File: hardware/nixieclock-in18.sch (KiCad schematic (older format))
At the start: 19 parts

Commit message: pcb begins
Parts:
- removed U?: TL071, symbol Amplifier_Operational:TL071
- added BT1: CR2032, Battery_Holders:Keystone_103_1x20mm-CoinCell, symbol Device:Battery_Cell
- added C1, C2, C3: 0.1, Capacitors_SMD:C_0805_HandSoldering, symbol Device:C
- added C4: 1.0, Capacitors_SMD:C_0805_HandSoldering, symbol Device:C
- added D1: LED, LEDs:LED_D3.0mm_FlatTop, symbol Device:LED
- added D4, D5, D6, D7: 3v3, Diodes_THT:D_DO-41_SOD81_P7.62mm_Horizontal, symbol Device:D_Zener
- added J1: PROG, Pin_Headers:Pin_Header_Straight_1x07_Pitch2.54mm, symbol Connector_Generic:Conn_01x06
- added J2: POWER, Connectors_Terminal_Blocks:TerminalBlock_bornier-2_P5.08mm, symbol Connector:Screw_Terminal_01x02
- added Q10, Q11, Q12, Q13, Q14, Q15, Q16, Q17, Q18, Q19, Q20, Q21, Q4, Q5, Q6, Q7, Q8, Q9: MPSA42, TO_SOT_Packages_SMD:SOT-23_Handsoldering, symbol Transistor_BJT:MPSA42
- added R1: 200, Resistors_SMD:R_0805_HandSoldering, symbol Device:R
- added R10, R12, R14, R15, R17, R19, R20, R21, R23, R25, R26, R28, R30, R9: 8k2, Resistors_SMD:R_0805_HandSoldering, symbol Device:R
- added R11, R16, R22, R27: 200k, Resistors_SMD:R_0805_HandSoldering, symbol Device:R
- added R13, R18, R24, R29: 27k, Resistors_SMD:R_0805_HandSoldering, symbol Device:R
- added R5: 10k, Resistors_SMD:R_0805_HandSoldering, symbol Device:R
- added T1, T2, T3, T4: IN18, in18:IN18, symbol in18:IN18
- added U1: LM1117-3.3, TO_SOT_Packages_SMD:SOT-223, symbol Regulator_Linear:LM1117-3.3
- added U2: DS3231M, Housings_SOIC:SOIC-16W_7.5x10.3mm_Pitch1.27mm, symbol Timer_RTC:DS3231M
- added U3: LM393, Housings_SOIC:SOIC-8_3.9x4.9mm_Pitch1.27mm, symbol Comparator:LM393
- C5, C6, C8: renamed from C?; footprint (none) -> Capacitors_SMD:C_0805_HandSoldering
- C7: renamed from C?; value 2.2uF -> 1.0; footprint (none) -> Capacitors_THT:CP_Radial_D10.0mm_P5.00mm
- D2: renamed from D?; footprint (none) -> Diodes_THT:D_A-405_P10.16mm_Horizontal
- D3: renamed from D?; footprint (none) -> Diodes_THT:D_DO-41_SOD81_P7.62mm_Horizontal
- L1: renamed from L?; footprint (none) -> Inductors_THT:L_Radial_D12.0mm_P6.00mm_MuRATA_1900R
- Q1, Q2: renamed from Q?; footprint Package_TO_SOT_SMD:SOT-23 -> TO_SOT_Packages_SMD:SOT-23_Handsoldering
- Q3: renamed from Q?; footprint Package_SO:PowerPAK_SO-8_Single -> Housings_SOIC:SOIC-8_3.9x4.9mm_Pitch1.27mm
- R2, R3, R4, R6: renamed from R?; footprint (none) -> Resistors_SMD:R_0805_HandSoldering
- R7, R8: renamed from R?; footprint (none) -> Resistors_THT:R_Axial_DIN0207_L6.3mm_D2.5mm_P10.16mm_Horizontal
- RV1: renamed from RV?; footprint (none) -> Potentiometers:Potentiometer_Trimmer_ACP_CA6v_Horizontal
- U4: renamed from U?; footprint RF_Module:ESP32-WROOM-32 -> ESP32-footprints-Lib:ESP32-WROOM
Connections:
- net +15V: now also C1.2, J2.1 (Pin_1), U1.3 (VI), U3.8 (V+)
- net +3V3: now also C2.2, C3.2, J1.1 (Pin_1), R5.1, U1.2 (VO), U2.2 (VCC)
- net 170V: now also R11.2, R13.2, R16.2, R18.2, R22.2, R24.2, R27.2, R29.2
- net GND: now also BT1.2 (-), C1.1, C2.1, C3.1, C4.1, D1.1 (K), D4.2 (A), D5.2 (A), D6.2 (A), D7.2 (A), J1.4 (Pin_4), J2.2 (Pin_2), Q10.1 (E), Q12.1 (E), Q13.1 (E), Q14.1 (E), Q15.1 (E), Q17.1 (E), Q18.1 (E), Q19.1 (E), Q21.1 (E), Q4.1 (E), Q5.1 (E), Q6.1 (E), Q8.1 (E), Q9.1 (E), U1.1 (GND), U2.10 (GND), U2.11 (GND), U2.12 (GND), U2.13 (GND), U2.5 (GND), U2.6 (GND), U2.7 (GND), U2.8 (GND), U2.9 (GND), U3.4 (V-)
- net PWM: now also U3.3 (+)
- net at R3.2, R4.1: now also U3.2 (-)
- net at Q1.1 (B), Q2.1 (B), R6.2: now also U3.1
- net I2C_SCL: now reaches U4.11 (IO26)
- net I2C_SCL: now also U2.16 (SCL)
- net I2C_SDA: now reaches U4.12 (IO27)
- net I2C_SDA: now also U2.15 (SDA)
- net IO0: now reaches U4.25 (IO0)
- net IO0: now also J1.3 (Pin_3)
- net EN: now reaches U4.3 (EN)
- net EN: now also C4.2, J1.2 (Pin_2), R5.2
- net UART_RX: now reaches U4.34 (RXD0/IO3)
- net UART_RX: now also J1.6 (Pin_6)
- net UART_TX: now reaches U4.35 (TXD0/IO1)
- net UART_TX: now also J1.5 (Pin_5)
- new net: Q7.1 (E), T1.12 (A), T1.4 (A)
- new net: D1.2 (A), R1.2
- new net: Q4.2 (B), R10.2
- new net: Q6.2 (B), R12.2
- new net: Q8.2 (B), R15.2
- new net: Q10.2 (B), R17.2
- new net: Q12.2 (B), R19.2
- new net: Q13.2 (B), R21.2
- new net: Q15.2 (B), R23.2
- new net: Q17.2 (B), R26.2
- new net: Q19.2 (B), R28.2
- new net: BT1.1 (+), U2.14 (VBAT)
- new net: Q21.2 (B), R30.2
- new net: Q11.1 (E), T2.12 (A), T2.4 (A)
- new net: Q16.1 (E), T3.12 (A), T3.4 (A)
- new net: Q20.1 (E), T4.12 (A), T4.4 (A)
- new net: Q5.3 (C), Q7.2 (B), R11.1
- new net: Q7.3 (C), R13.1
- new net: Q5.2 (B), R9.2
- new net: Q11.2 (B), Q9.3 (C), R16.1
- new net: Q11.3 (C), R18.1
- new net: Q9.2 (B), R14.2
- new net: Q14.3 (C), Q16.2 (B), R22.1
- new net: Q16.3 (C), R24.1
- new net: Q14.2 (B), R20.2
- new net: Q18.3 (C), Q20.2 (B), R27.1
- new net: Q20.3 (C), R29.1
- new net: Q18.2 (B), R25.2
- new net CAT0: Q4.3 (C), T1.13 (D0), T2.13 (D0), T3.13 (D0), T4.13 (D0)
- new net CAT1: Q6.3 (C), T1.11 (D1), T2.11 (D1), T3.11 (D1), T4.11 (D1)
- new net CAT2: Q8.3 (C), T1.10 (D2), T2.10 (D2), T3.10 (D2), T4.10 (D2)
- new net CAT3: Q10.3 (C), T1.7 (D3), T2.7 (D3), T3.7 (D3), T4.7 (D3)
- new net CAT4: Q12.3 (C), T1.2 (D4), T2.2 (D4), T3.2 (D4), T4.2 (D4)
- new net CAT5: Q13.3 (C), T1.3 (D5), T2.3 (D5), T3.3 (D5), T4.3 (D5)
- new net CAT6: Q15.3 (C), T1.5 (D6), T2.5 (D6), T3.5 (D6), T4.5 (D6)
- new net CAT7: Q17.3 (C), T1.6 (D7), T2.6 (D7), T3.6 (D7), T4.6 (D7)
- new net CAT8: Q19.3 (C), T1.9 (D8), T2.9 (D8), T3.9 (D8), T4.9 (D8)
- new net CAT9: Q21.3 (C), T1.14 (D9), T2.14 (D9), T3.14 (D9), T4.14 (D9)
- new net DIG0: R10.1
- new net DIG1: R12.1
- new net DIG2: R15.1
- new net DIG3: R17.1
- new net DIG4: R19.1
- new net DIG5: R21.1
- new net DIG6: R23.1
- new net DIG7: R26.1
- new net DIG8: R28.1
- new net DIG9: R30.1
- new net LED_SYNC: R1.1
- new net ~AN0: D4.1 (K), R9.1
- new net ~AN1: D5.1 (K), R14.1
- new net ~AN2: D6.1 (K), R20.1
- new net ~AN3: D7.1 (K), R25.1
- no-connect marks 2 -> 5
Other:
- moved on the sheet: C5, C6, C7, C8, D2, D3, L1, Q1, Q2, Q3, R2, R3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

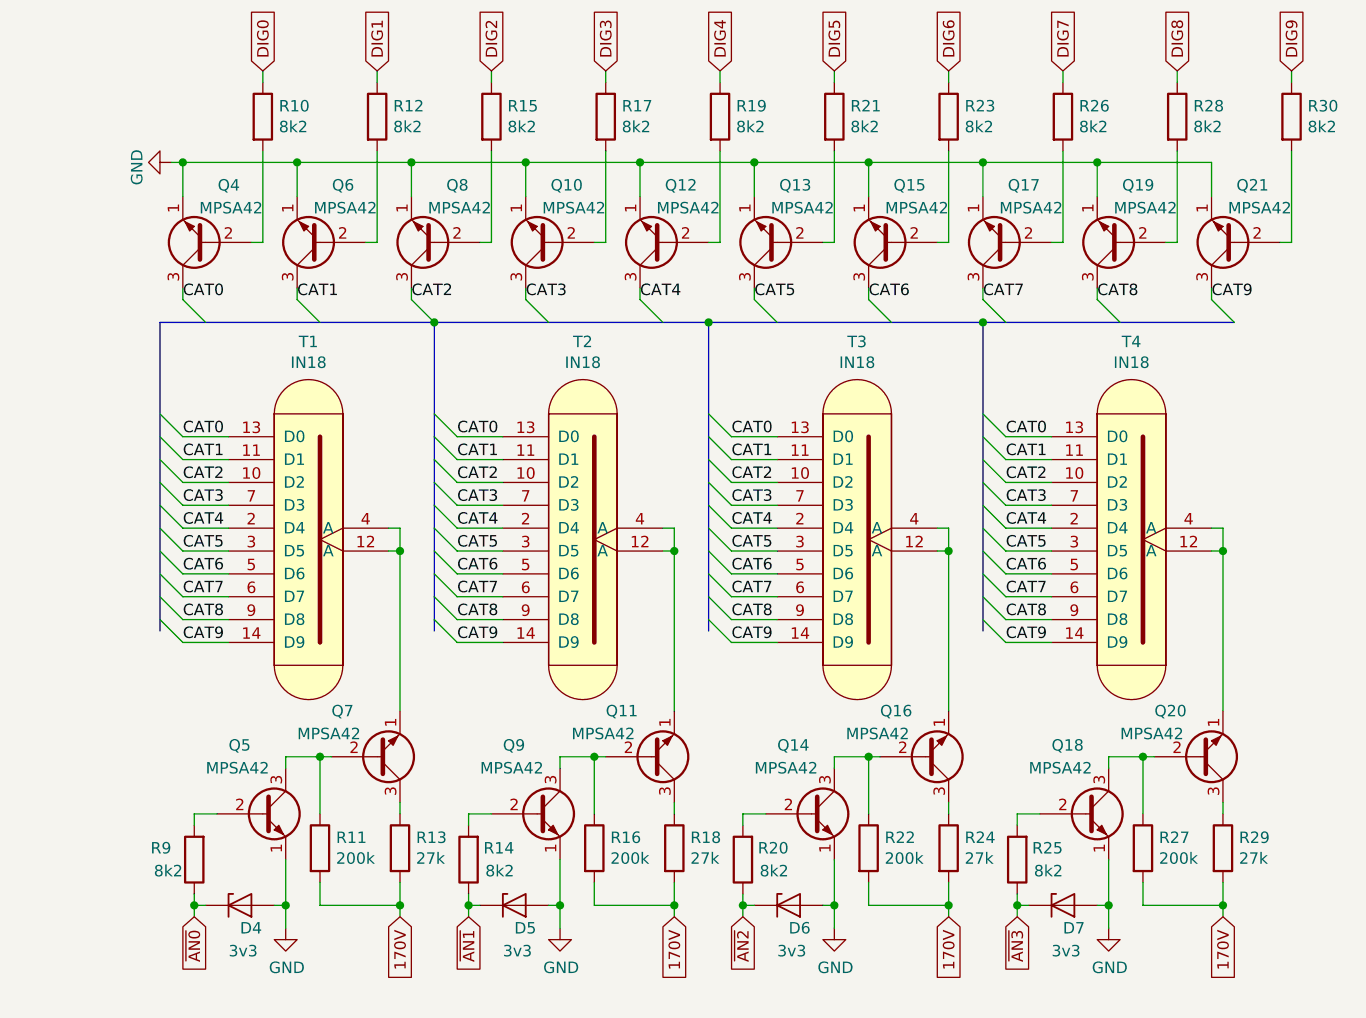
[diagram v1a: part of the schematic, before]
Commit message: fix mmbta42 pinout
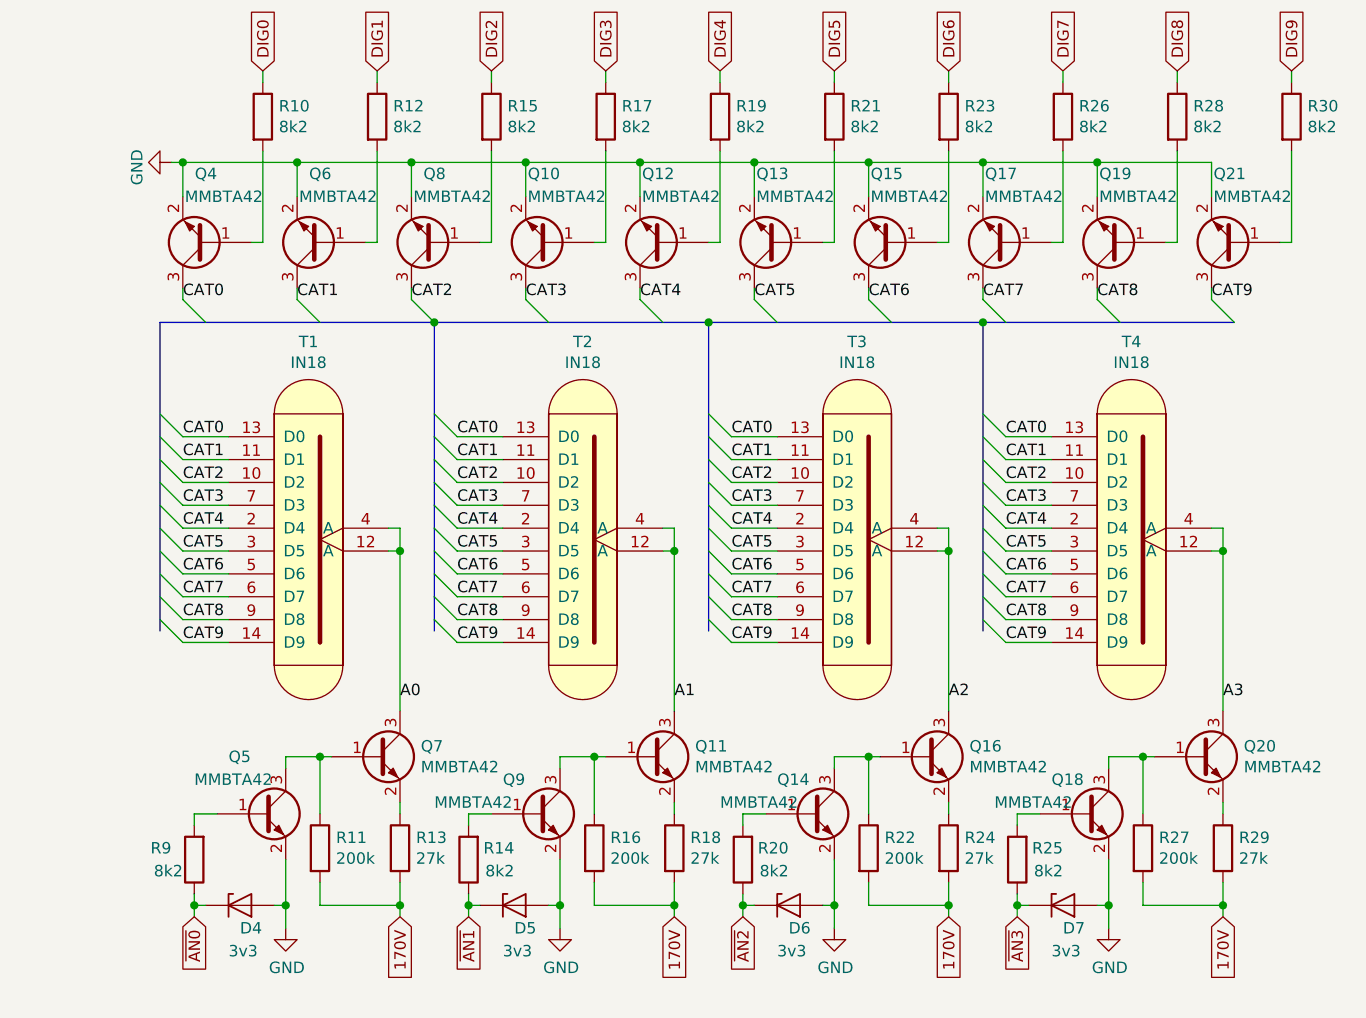
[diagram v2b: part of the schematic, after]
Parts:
- removed Q10, Q11, Q12, Q13, Q14, Q15, Q16, Q17, Q18, Q19, Q20, Q21, Q4, Q5, Q6, Q7, Q8, Q9: MPSA42, TO_SOT_Packages_SMD:SOT-23_Handsoldering, symbol Transistor_BJT:MPSA42
- added Q10, Q11, Q12, Q13, Q14, Q15, Q16, Q17, Q18, Q19, Q20, Q21, Q4, Q5, Q6, Q7, Q8, Q9: MMBTA42, TO_SOT_Packages_SMD:SOT-23_Handsoldering, symbol Transistor_BJT:BC848
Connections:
- net CAT0: now also Q4.3 (C)
- net CAT1: now also Q6.3 (C)
- net CAT2: now also Q8.3 (C)
- net CAT3: now also Q10.3 (C)
- net CAT4: now also Q12.3 (C)
- net CAT5: now also Q13.3 (C)
- net CAT6: now also Q15.3 (C)
- net CAT7: now also Q17.3 (C)
- net CAT8: now also Q19.3 (C)
- net CAT9: now also Q21.3 (C)
- net GND: now also Q10.2 (E), Q12.2 (E), Q13.2 (E), Q14.2 (E), Q15.2 (E), Q17.2 (E), Q18.2 (E), Q19.2 (E), Q21.2 (E), Q4.2 (E), Q5.2 (E), Q6.2 (E), Q8.2 (E), Q9.2 (E)
- net A0: now reaches T1.12 (A), T1.4 (A)
- net A0: now also Q7.3 (C)
- net at R10.2: now also Q4.1 (B)
- net at R12.2: now also Q6.1 (B)
- net at R15.2: now also Q8.1 (B)
- net at R17.2: now also Q10.1 (B)
- net at R19.2: now also Q12.1 (B)
- net at R21.2: now also Q13.1 (B)
- net at R23.2: now also Q15.1 (B)
- net at R26.2: now also Q17.1 (B)
- net at R28.2: now also Q19.1 (B)
- net at R30.2: now also Q21.1 (B)
- net A1: now reaches T2.12 (A), T2.4 (A)
- net A1: now also Q11.3 (C)
- net A2: now reaches T3.12 (A), T3.4 (A)
- net A2: now also Q16.3 (C)
- net A3: now reaches T4.12 (A), T4.4 (A)
- net A3: now also Q20.3 (C)
- net at R11.1: now also Q5.3 (C), Q7.1 (B)
- net at R13.1: now also Q7.2 (E)
- net at R9.2: now also Q5.1 (B)
- net at R16.1: now also Q11.1 (B), Q9.3 (C)
- net at R18.1: now also Q11.2 (E)
- net at R14.2: now also Q9.1 (B)
- net at R22.1: now also Q14.3 (C), Q16.1 (B)
- net at R24.1: now also Q16.2 (E)
- net at R20.2: now also Q14.1 (B)
- net at R27.1: now also Q18.3 (C), Q20.1 (B)
- net at R29.1: now also Q20.2 (E)
- net at R25.2: now also Q18.1 (B)

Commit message: finished pcb
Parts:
- added F1: 100mA, Resistors_SMD:R_0805_HandSoldering, symbol Device:Fuse
- J1: footprint Pin_Headers:Pin_Header_Straight_1x07_Pitch2.54mm -> Pin_Headers:Pin_Header_Straight_1x06_Pitch2.54mm
- Q3: footprint Housings_SOIC:SOIC-8_3.9x4.9mm_Pitch1.27mm -> Housings_SOIC:PowerPAK_SO-8_Single
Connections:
- net +15V: now also F1.2; no longer J2.1 (Pin_1)
- net DIG0: now also U4.21 (SDO/SD0)
- net DIG1: now also U4.26 (IO4)
- net DIG2: now also U4.23 (IO15)
- net DIG3: now also U4.19 (SCS/CMD)
- net DIG4: now also U4.27 (IO16)
- net DIG5: now also U4.17 (SHD/SD2)
- net DIG6: now also U4.18 (SWP/SD3)
- net DIG7: now also U4.28 (IO17)
- net DIG8: now also U4.22 (SDI/SD1)
- net DIG9: now also U4.31 (IO19)
- net LED_SYNC: now also U4.37 (IO23)
- net ~AN0: now also U4.8 (IO32)
- net ~AN1: now also U4.7 (IO35)
- net ~AN2: now also U4.36 (IO22)
- net ~AN3: now also U4.33 (IO21)
- new net: F1.1, J2.1 (Pin_1)
- no-connect marks 5 -> 13
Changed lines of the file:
@@
 	3500 6850 4200 6850
-$Comp
-L RF_Module:ESP32-WROOM-32D U4
-U 1 1 5D6FCD20
-P 3800 2550
-F 0 "U4" H 3350 4100 50  0000 C CNN
-F 1 "ESP32-WROOM-32D" H 3350 4000 50  0000 C CNN
-F 2 "ESP32-footprints-Lib:ESP32-WROOM" H 3800 1050 50  0001 C CNN
-F 3 "https://www.espressif.com/sites/default/files/documentation/esp32-wroom-32d_esp32-wroom-32u_datasheet_en.pdf" H 3500 2600 50  0001 C CNN
-	1    3800 2550
-	1    0    0    -1
-$EndComp
 $Comp
 L power:GND #PWR0103
@@
 F 0 "Q3" H 4306 6346 50  0000 L CNN
 F 1 "Si4434" H 4306 6255 50  0000 L CNN
-F 2 "Housings_SOIC:SOIC-8_3.9x4.9mm_Pitch1.27mm" H 4300 6225 50  0001 L CIN
+F 2 "Housings_SOIC:PowerPAK_SO-8_Single" H 4300 6225 50  0001 L CIN
 F 3 "https://www.vishay.com/docs/73152/si7336adp.pdf" H 4100 6300 50  0001 L CNN
 	1    4100 6300
@@
 F 0 "J1" H 2580 3992 50  0000 L CNN
 F 1 "PROG" H 2580 3901 50  0000 L CNN
-F 2 "Pin_Headers:Pin_Header_Straight_1x07_Pitch2.54mm" H 2500 4000 50  0001 C CNN
+F 2 "Pin_Headers:Pin_Header_Straight_1x06_Pitch2.54mm" H 2500 4000 50  0001 C CNN
 F 3 "~" H 2500 4000 50  0001 C CNN
 	1    2500 4000
@@
 L power:+15V #PWR0127
 U 1 1 5D6C49C6
-P 2150 4700
-F 0 "#PWR0127" H 2150 4550 50  0001 C CNN
-F 1 "+15V" H 2165 4873 50  0000 C CNN
-F 2 "" H 2150 4700 50  0001 C CNN
-F 3 "" H 2150 4700 50  0001 C CNN
-	1    2150 4700
+P 1750 4700
+F 0 "#PWR0127" H 1750 4550 50  0001 C CNN
+F 1 "+15V" H 1765 4873 50  0000 C CNN
+F 2 "" H 1750 4700 50  0001 C CNN
+F 3 "" H 1750 4700 50  0001 C CNN
+	1    1750 4700
 	0    -1   -1   0
 $EndComp
@@
 	-1   0    0    1
 $EndComp
+Text GLabel 4500 2950 2    50   Input ~ 0
+LED_SYNC
+Wire Wire Line
+	4400 2950 4500 2950
+Text GLabel 4500 2850 2    50   Input ~ 0
+~AN2
+Wire Wire Line
+	4500 2850 4400 2850
+$Comp
+L RF_Module:ESP32-WROOM-32D U4
+U 1 1 5D6FCD20
+P 3800 2550
+F 0 "U4" H 3350 4100 50  0000 C CNN
+F 1 "ESP32-WROOM-32D" H 3350 4000 50  0000 C CNN
+F 2 "ESP32-footprints-Lib:ESP32-WROOM" H 3800 1050 50  0001 C CNN
+F 3 "https://www.espressif.com/sites/default/files/documentation/esp32-wroom-32d_esp32-wroom-32u_datasheet_en.pdf" H 3500 2600 50  0001 C CNN
+	1    3800 2550
+	1    0    0    -1
+$EndComp
+Text GLabel 4500 2750 2    50   Input ~ 0
+~AN3
+Wire Wire Line
+	4500 2750 4400 2750
+Text GLabel 4500 3650 2    50   Input ~ 0
+~AN1
+Wire Wire Line
+	4500 3650 4400 3650
+Text GLabel 4500 3350 2    50   Input ~ 0
+~AN0
+Wire Wire Line
+	4500 3350 4400 3350
+Text GLabel 4500 2650 2    50   Input ~ 0
+DIG9
+Wire Wire Line
+	4500 2650 4400 2650
+Text GLabel 4500 1750 2    50   Input ~ 0
+DIG1
+Wire Wire Line
+	4500 1750 4400 1750
+Text GLabel 4500 2450 2    50   Input ~ 0
+DIG7
+Wire Wire Line
+	4500 2450 4400 2450
+Text GLabel 4500 2350 2    50   Input ~ 0
+DIG4
+Wire Wire Line
+	4400 2350 4500 2350
+Text GLabel 4500 2250 2    50   Input ~ 0
+DIG2
+Wire Wire Line
+	4500 2250 4400 2250
+Text GLabel 3100 2650 0    50   Input ~ 0
+DIG8
+Wire Wire Line
+	3200 2650 3100 2650
+Text GLabel 3100 2550 0    50   Input ~ 0
+DIG0
+Wire Wire Line
+	3200 2550 3100 2550
+Text GLabel 3100 2750 0    50   Input ~ 0
+DIG5
+Wire Wire Line
+	3100 2750 3200 2750
+Text GLabel 3100 2850 0    50   Input ~ 0
+DIG6
+Wire Wire Line
+	3100 2850 3200 2850
+Text GLabel 3100 3050 0    50   Input ~ 0
+DIG3
+Wire Wire Line
+	3100 3050 3200 3050
+NoConn ~ 3200 2950
+NoConn ~ 4400 1550
+NoConn ~ 4400 1850
+NoConn ~ 4400 1950
+NoConn ~ 4400 2050
+NoConn ~ 4400 2150
+NoConn ~ 4400 3050
+NoConn ~ 4400 3450
+$Comp
+L Device:Fuse F1
+U 1 1 5D6F9D25
+P 2000 4700
+F 0 "F1" V 1803 4700 50  0000 C CNN
+F 1 "100mA" V 1894 4700 50  0000 C CNN
+F 2 "Resistors_SMD:R_0805_HandSoldering" V 1930 4700 50  0001 C CNN
+F 3 "~" H 2000 4700 50  0001 C CNN
+	1    2000 4700
+	0    1    1    0
+$EndComp
+Wire Wire Line
+	1850 4700 1750 4700
 Wire Bus Line
 	5750 2100 6950 2100

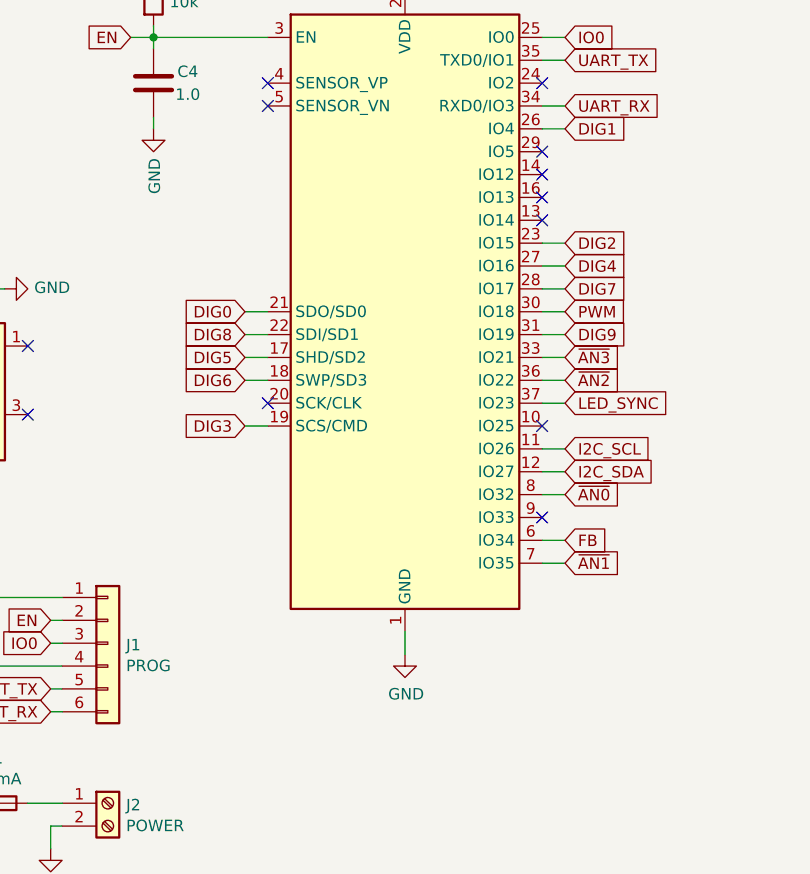
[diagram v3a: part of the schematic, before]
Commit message: change DIG5 pin (programmin flash issue)
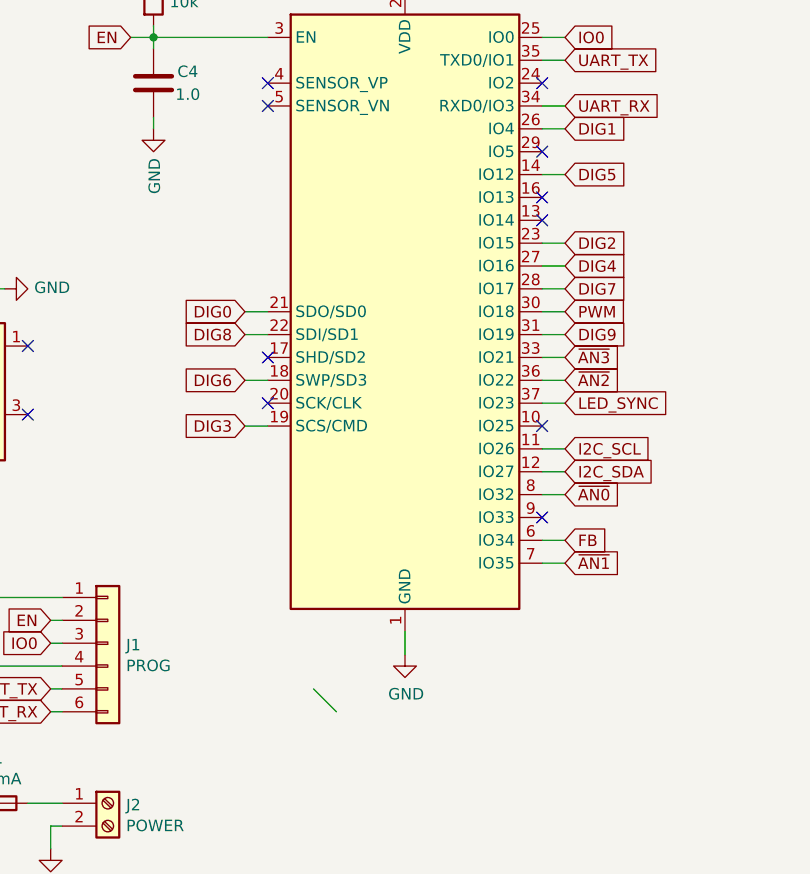
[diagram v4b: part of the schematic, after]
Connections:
- net DIG5: now also U4.14 (IO12); no longer U4.17 (SHD/SD2)
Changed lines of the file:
@@
 Wire Wire Line
 	3200 2550 3100 2550
-Text GLabel 3100 2750 0    50   Input ~ 0
+Text GLabel 4500 1950 2    50   Input ~ 0
 DIG5
-Wire Wire Line
-	3100 2750 3200 2750
 Text GLabel 3100 2850 0    50   Input ~ 0
 DIG6
@@
 NoConn ~ 4400 1550
 NoConn ~ 4400 1850
-NoConn ~ 4400 1950
 NoConn ~ 4400 2050
-NoConn ~ 4400 2150
 NoConn ~ 4400 3050
 NoConn ~ 4400 3450
@@
 Wire Wire Line
 	1850 4700 1750 4700
+Entry Wire Line
+	3400 4200 3500 4300
+Wire Wire Line
+	4400 1950 4500 1950
+NoConn ~ 3200 2750
+NoConn ~ 4400 2150
 Wire Bus Line
 	5750 2100 6950 2100
